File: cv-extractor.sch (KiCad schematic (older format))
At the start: 25 parts, among them J1 mono-jack, J2 mono-jack, J3 power_connector_10pos, U1 TL074

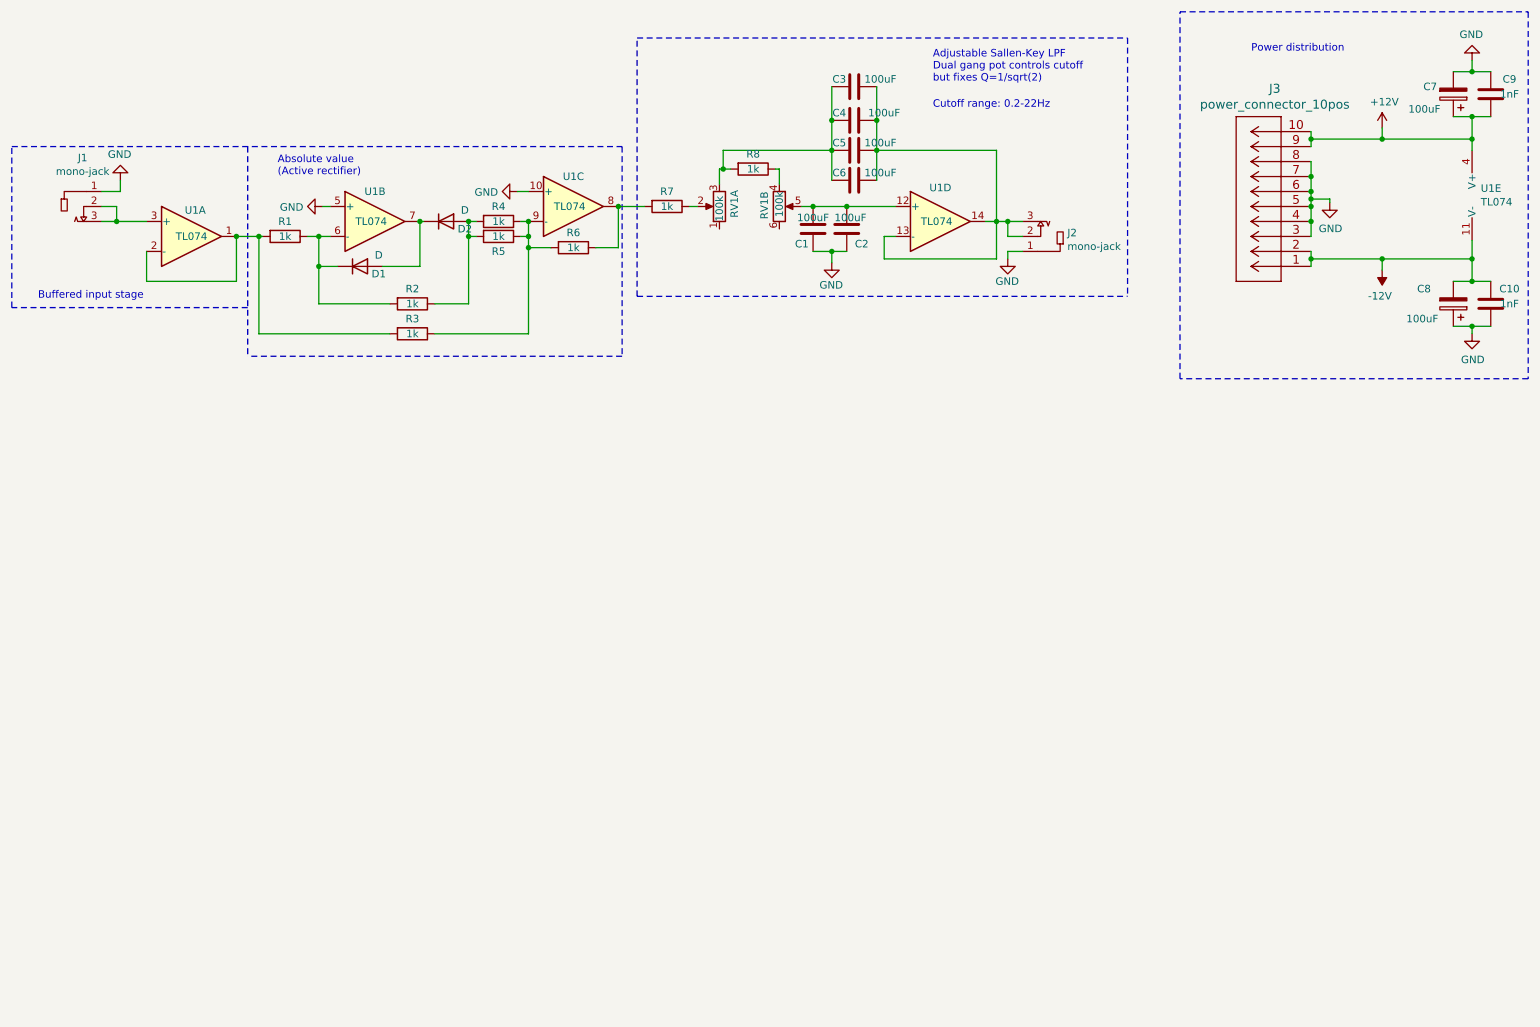
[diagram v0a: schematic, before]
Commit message: narrower profile, added test points, reduced cutoff range, V2 for fab
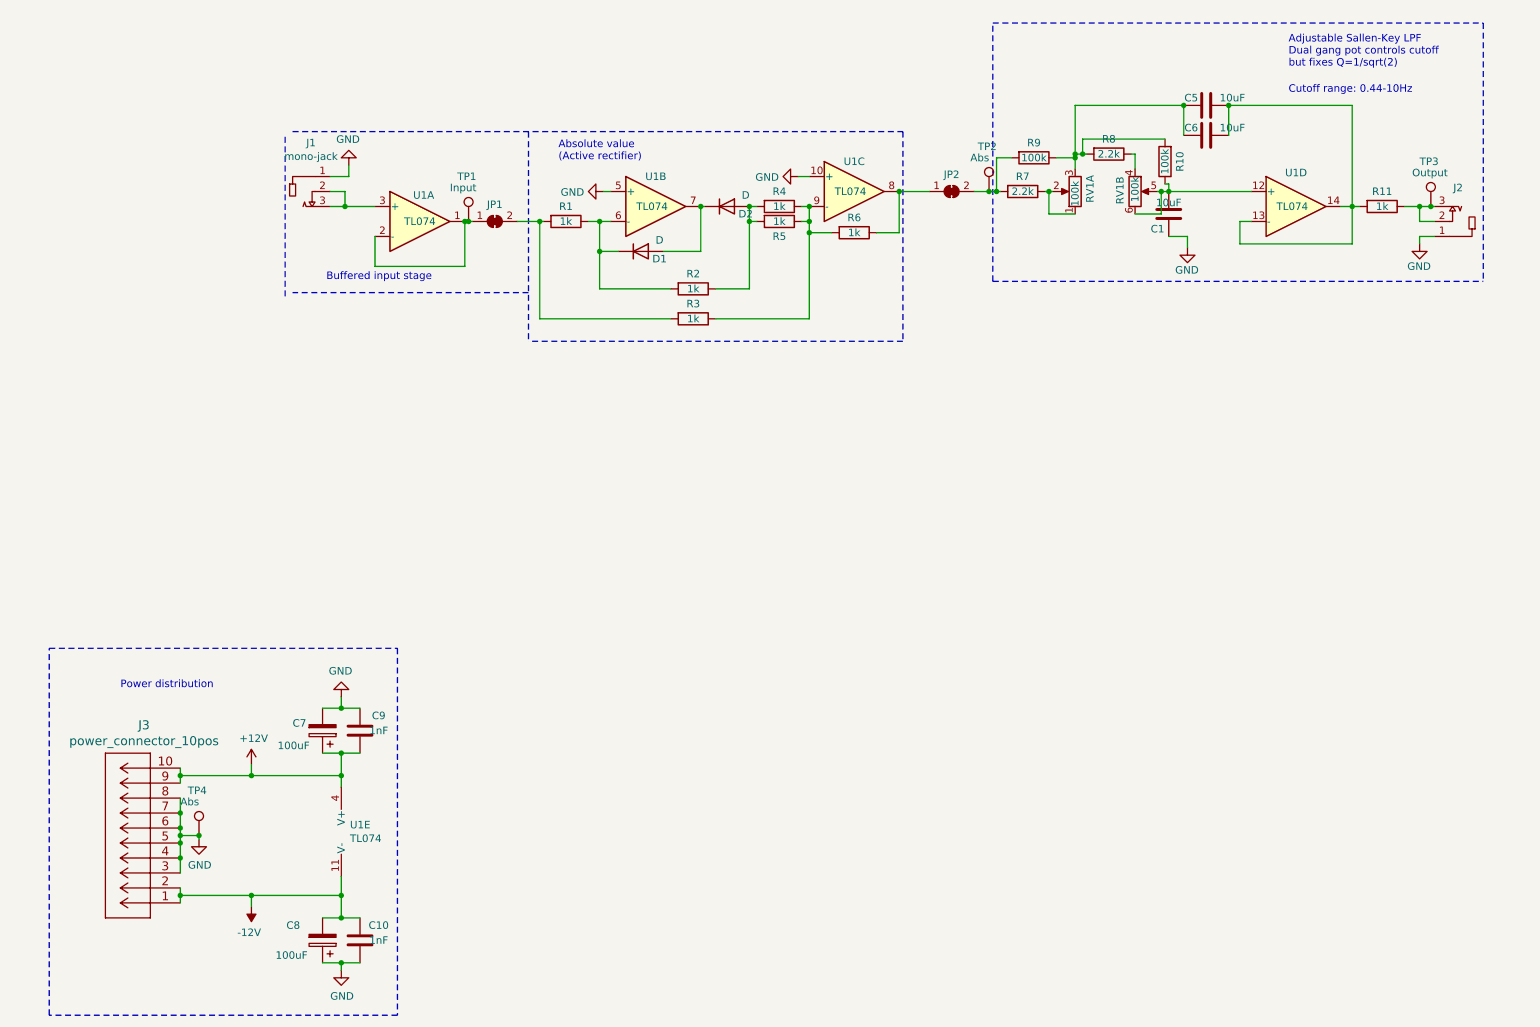
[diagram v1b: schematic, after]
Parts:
- removed C2, C3, C4: 100uF, Capacitor_SMD:C_1206_3216Metric, symbol Device:C
- added JP1, JP2: SolderJumper_2_Bridged, Jumper:SolderJumper-2_P1.3mm_Open_RoundedPad1.0x1.5mm, symbol Jumper:SolderJumper_2_Bridged
- added R10, R9: 100k, Resistor_SMD:R_0603_1608Metric, symbol Device:R
- added R11: 1k, Resistor_SMD:R_0603_1608Metric, symbol Device:R
- added TP1: Input, matterwave:TestPoint_TP107, symbol Connector:TestPoint
- added TP2, TP4: Abs, matterwave:TestPoint_TP107, symbol Connector:TestPoint
- added TP3: Output, matterwave:TestPoint_TP107, symbol Connector:TestPoint
- C1, C5, C6: value 100uF -> 10uF; footprint Capacitor_SMD:C_1206_3216Metric -> Capacitor_SMD:C_0603_1608Metric; JLCPCB CL31A107MQHNNNE -> C344022
- C10, C9: JLCPCB CL10B102KB8NNNC -> C1588
- C7, C8: JLCPCB VES101M1ETR-0607 -> C176675
- D1, D2: footprint Diode_SMD:D_SMA -> Diode_SMD:D_SOD-323F; JLCPCB M7 -> C2128
- R1, R2, R3, R4, R5, R6: JLCPCB TC0325F1001T5E -> C21190
- R7, R8: value 1k -> 2.2k; JLCPCB TC0325F1001T5E -> C4190
- U1: JLCPCB TL074IDR -> C12594
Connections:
- net GND: now also TP4.1
- net at U1.1, U1.2 (-): now also JP1.1 (A), TP1.1; no longer R1.2, R3.2
- net at R6.1, U1.8: now also JP2.1 (A); no longer R7.2
- net at C1.2, RV1.5, U1.12 (+): now also RV1.6, R10.1
- net at C5.2, C6.2, U1.13 (-)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: now also R11.2; no longer J2.2, J2.3
- net at C5.1, C6.1, R8.2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: now also R10.2, R9.1
- net at R7.1, RV1.2: now also RV1.1
- new net: JP1.2 (B), R1.2, R3.2
- new net: J2.2, J2.3, R11.1, TP3.1
- new net: JP2.2 (B), R7.2, R9.2, TP2.1
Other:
- note added: "Cutoff range: 0.44-10Hz"
- note removed: "Cutoff range: 0.2-22Hz"
- moved on the sheet: C1, C10, C5, C6, C7, C8, C9, D1, D2, J1, J2, J3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

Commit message: havent been good about commits, its at V4 now
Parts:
- removed R10: 100k, Resistor_SMD:R_0603_1608Metric, symbol Device:R
- removed R11: 1k, Resistor_SMD:R_0603_1608Metric, symbol Device:R
- added H1, H2: Hole, MountingHole:MountingHole_3.2mm_M3, symbol matterwave:Hole
- added R12: 1k, Resistor_SMD:R_0603_1608Metric, symbol Device:R
- added RD1: 1M, Resistor_SMD:R_0603_1608Metric, symbol Device:R
- added RV2, RV3: 10k, matterwave:pot_bourns_PTV09, symbol Device:R_POT
- C1, C5, C6: value 10uF -> 470nF; JLCPCB C344022 -> C1623
- J1: value mono-jack -> Wave In
- J2: value mono-jack -> CV Out
- J3: symbol synth-components:power_connector_10pos -> cv-extractor-rescue:power_connector_10pos-synth-components
- R7, R8: value 2.2k -> 1k; JLCPCB C4190 -> C21190
- R9: value 100k -> 1k; JLCPCB C25803 -> C21190
- TP4: value Abs -> GND
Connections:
- net GND: now also R9.1, R12.1, RD1.1
- net at JP1.1 (A), TP1.1, U1.1: now also RV2.1; no longer U1.2 (-)
- net at J1.2, J1.3, U1.3 (+): now also RD1.2
- net at C5.2, C6.2, U1.14: now also J2.2, J2.3, TP3.1, RV3.3; no longer U1.13 (-)
- net at C5.1, C6.1, R8.2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: no longer R9.1
- net at JP2.2 (B), R7.2, TP2.1: no longer R9.2
- new net: R12.2, RV2.2, RV2.3, U1.2 (-)
- new net: RV3.2, U1.13 (-)
- new net: R9.2, RV3.1
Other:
- moved on the sheet: J1, J2, TP3
